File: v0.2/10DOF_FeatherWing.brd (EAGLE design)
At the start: 22.9 x 50.8 mm, 17 parts

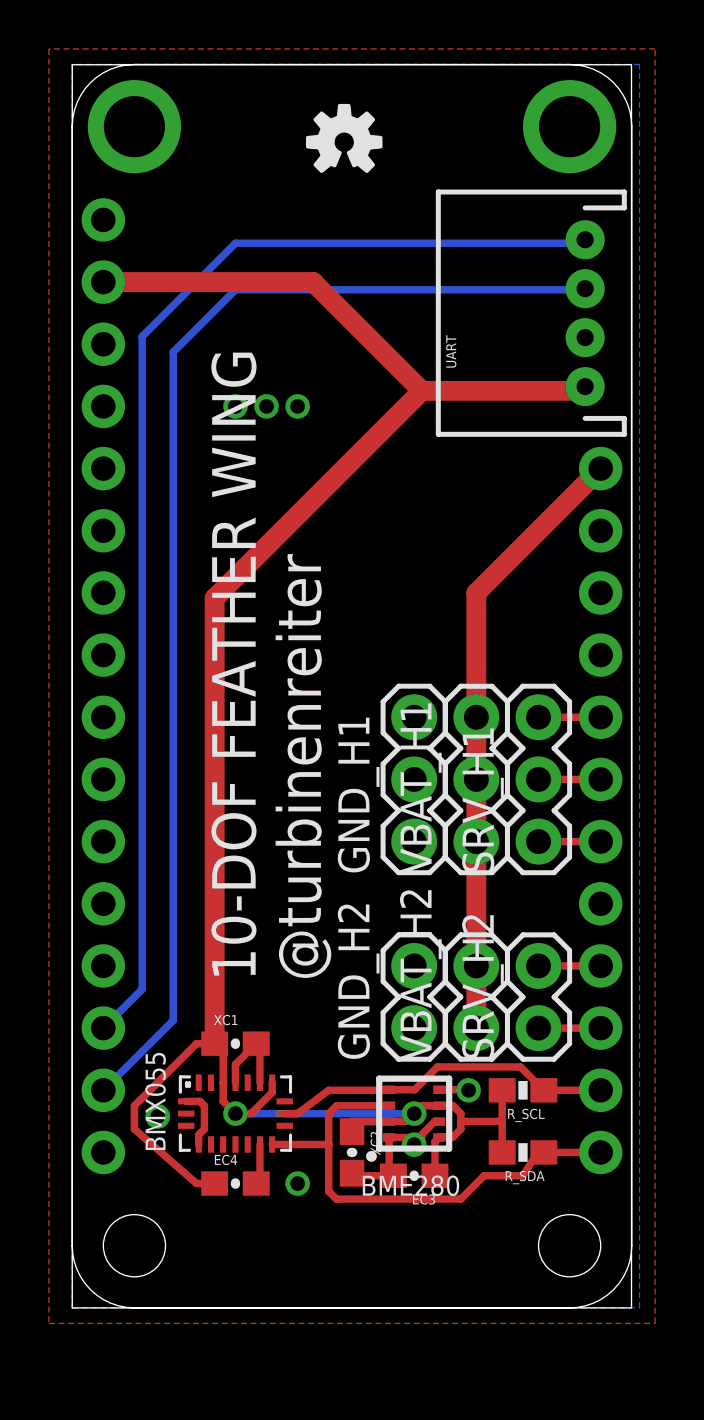
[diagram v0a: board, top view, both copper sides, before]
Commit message: updatet v2 with more servo headers, better routing
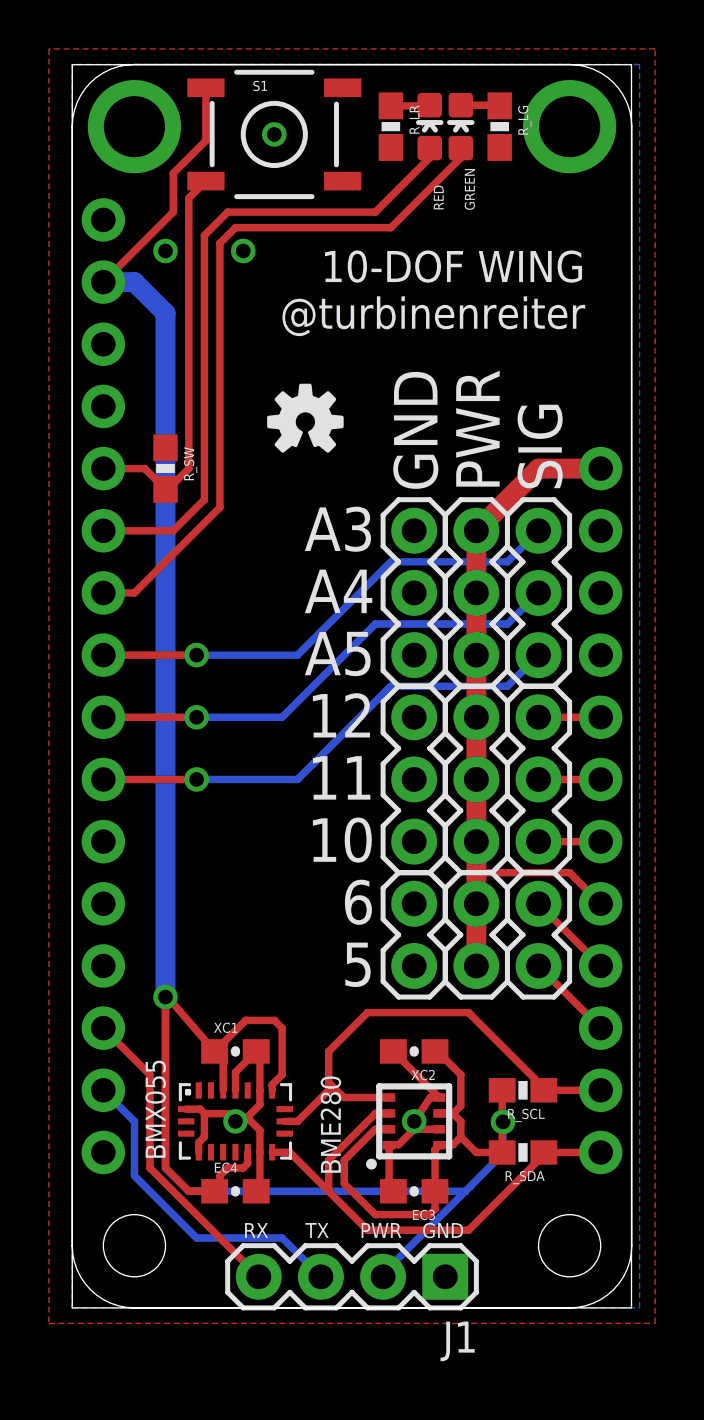
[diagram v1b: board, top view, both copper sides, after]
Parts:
- removed UART: (no value), SparkFun-Connectors:JST-4-PTH
- added GND_H3, SRV_H3, VBAT_H3: (no value), SparkFun-Connectors:1X03
- added GREEN: GREEN, SparkFun-LED:LED-0603
- added J1: (no value), SparkFun-Connectors:1X04
- added RED: RED, SparkFun-LED:LED-0603
- added R_LG, R_LR: 82, SparkFun-Resistors:0603-RES
- added R_SW: 10K, SparkFun-Resistors:0603-RES
- added S1: SWITCH-MOMENTARY-2SMD, SparkFun-Electromechanical:TACTILE-SWITCH-SMD
- moved LOGO1 11.5 mm to (9.53, 36.2)
- moved XC2 4.85 mm to (14.0, 10.5), turned to 180 degrees
- moved GND_H2 2.54 mm to (14.0, 14.0)
- moved SRV_H2 2.54 mm to (19.1, 14.0)
- moved VBAT_H2 2.54 mm to (16.5, 14.0)
- moved EC3 0.63 mm to (14.0, 4.76)
- moved XC1 0.32 mm to (6.67, 10.5)
- moved BME280 0.32 mm to (14.0, 7.62)
- moved BMX055 0.32 mm to (6.67, 7.62)
- moved EC4 0.32 mm to (6.67, 4.76)
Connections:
- removed net N$3: BMX055.13
- new net GREEN: GREEN.A, MS1.7
- new net N$4: GREEN.C, R_LG.1
- new net N$5: RED.C, R_LR.1
- new net RED: MS1.6, RED.A
- new net SRV6: MS1.10, SRV_H3.1
- new net SRV7: MS1.9, SRV_H3.2
- new net SRV8: MS1.8, SRV_H3.3
- new net SW1: MS1.5, R_SW.2, S1.3
- net 3.3V: now also BMX055.13, J1.2, S1.1; no longer UART.1
- net GND: now also GND_H3.1, GND_H3.2, GND_H3.3, J1.1, R_LG.2, R_LR.2, R_SW.1; no longer UART.2
- net RX: now also J1.4; no longer UART.4
- net TX: now also J1.3; no longer UART.3
- net VBAT: now also MS1.21, VBAT_H3.1, VBAT_H3.2, VBAT_H3.3
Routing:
- net TX: track 49.2 -> 13.3 mm
- net RX: track 48.6 -> 12.8 mm
- net GREEN: track 0.00 -> 28.7 mm
- net RED: track 0.00 -> 26.4 mm
- net 3.3V: track 88.6 -> 112.9 mm
- net SRV6: track 0.00 -> 19.9 mm, vias 0 -> 1
- net SRV8: track 0.00 -> 19.9 mm, vias 0 -> 1
- net SRV7: track 0.00 -> 19.9 mm, vias 0 -> 1
- net SW1: track 0.00 -> 16.2 mm
- net GND: track 15.1 -> 21.4 mm, vias 7 -> 5
- net SCL: track 14.0 -> 19.8 mm
- net VBAT: track 25.0 -> 29.5 mm
- net N$5: track 0.00 -> 1.60 mm
- net N$4: track 0.00 -> 1.60 mm
- net SRV2: track 2.54 -> 3.59 mm
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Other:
- board text added: "10"
- board text added: "10-DOF WING @turbinenreiter"
- board text added: "11"
- board text added: "12"
- board text added: "5"
- board text added: "6"
- board text added: "A3"
- board text added: "A4"
- board text added: "A5"
- board text added: "GND"
- board text added: "PWR"
- board text added: "RX"
- board text added: "SIG"
- board text added: "TX"
- board text removed: "10-DOF FEATHER WING @turbinenreiter"

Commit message: added SPI header
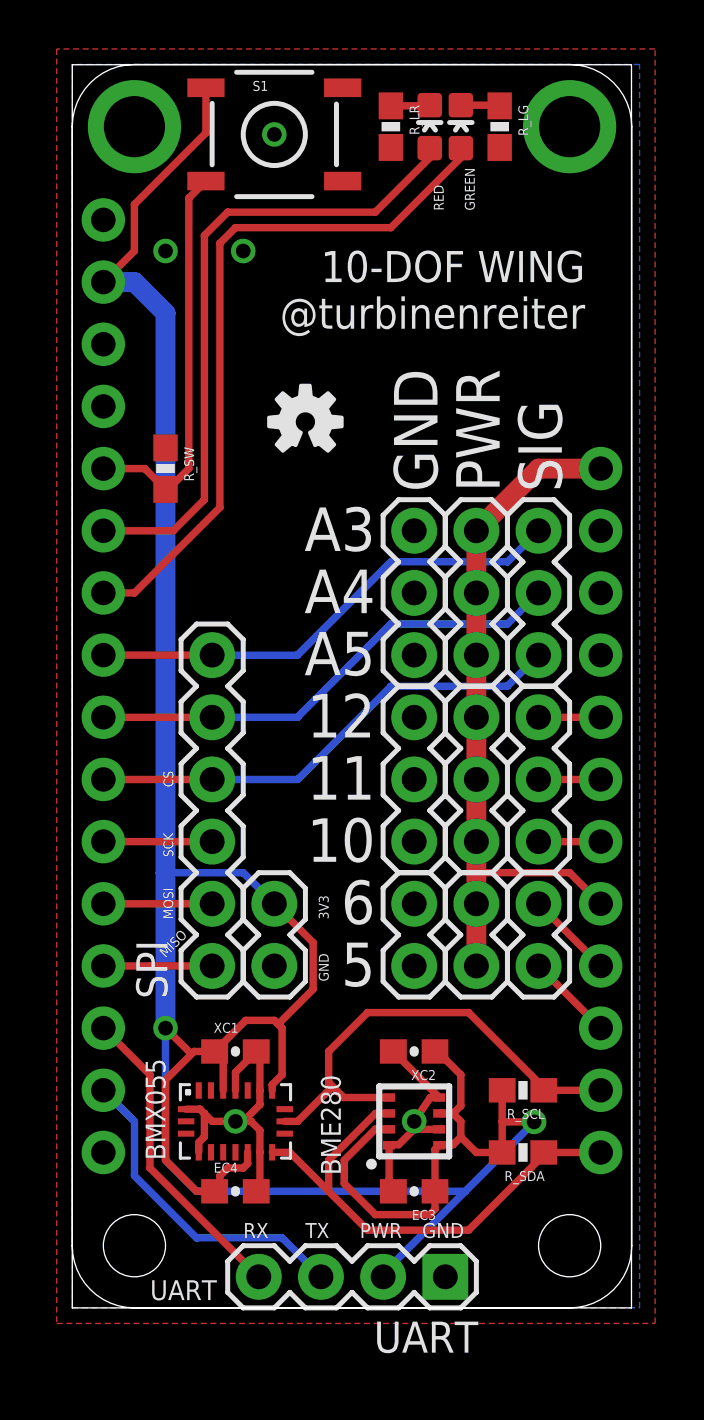
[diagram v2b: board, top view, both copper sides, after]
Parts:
- added SPI: FEMALE 2x3, SparkFun-Connectors:1X06
- added UART: (no value), SparkFun-Connectors:1X04
- J1: device SparkFun-Connectors:1X04 -> SparkFun-Connectors:1X02
- moved J1 14.5 mm to (8.26, 14.0), turned to 90 degrees
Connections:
- new net MISO: MS1.13, SPI.1
- new net MOSI: MS1.12, SPI.2
- new net SCK: MS1.11, SPI.3
- net 3.3V: now also UART.2
- net GND: now also UART.1
- net RX: now also UART.4; no longer J1.4
- net SRV6: now also SPI.4
- net SRV7: now also SPI.5
- net SRV8: now also SPI.6
- net TX: now also UART.3; no longer J1.3
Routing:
- net 3.3V: track 112.9 -> 122.7 mm
- net SCK: track 0.00 -> 4.45 mm
- net MOSI: track 0.00 -> 4.45 mm
- net MISO: track 0.00 -> 4.45 mm
- net SRV8: vias 1 -> 0
- net SRV7: vias 1 -> 0
- net SRV6: vias 1 -> 0
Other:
- board text added: "3V3"
- board text added: "CS"
- board text added: "MISO"
- board text added: "MOSI"
- board text added: "SCK"
- board text added: "UART"
